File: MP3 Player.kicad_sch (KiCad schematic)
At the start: 48 parts, among them J1 Conn_01x02_Pin, J2 USB_C_Receptacle_USB2.0_14P, J3 SJ2-3574A-SMT-TR, J4 Conn_01x02_Pin, J5 1051620001, J6 Conn_01x04_Pin, Q1 IRLML6402, SW1 SW_SPDT, SW2 SW_MEC_5E, SW3 SW_MEC_5E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

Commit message: Cleaned up the schematic
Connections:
- net +3V3: no longer SW5.3 (K), SW5.4 (A), SW6.3 (K), SW6.4 (A), SW7.3 (K), SW7.4 (A), SW8.3 (K), SW8.4 (A)
- net HPL: no longer C7.1, J3.2
- net HRP: no longer C8.1, J3.3
- new net: SW7.3 (K), SW7.4 (A)
- new net: C7.1, J3.2
- new net: SW5.3 (K), SW5.4 (A)
- new net: SW6.3 (K), SW6.4 (A)
- new net: SW8.3 (K), SW8.4 (A)
- new net: C8.1, J3.3
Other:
- moved on the sheet: C7, C8, J6, R10, R11, R12, R13, R14, SW4, SW5, SW6, SW7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

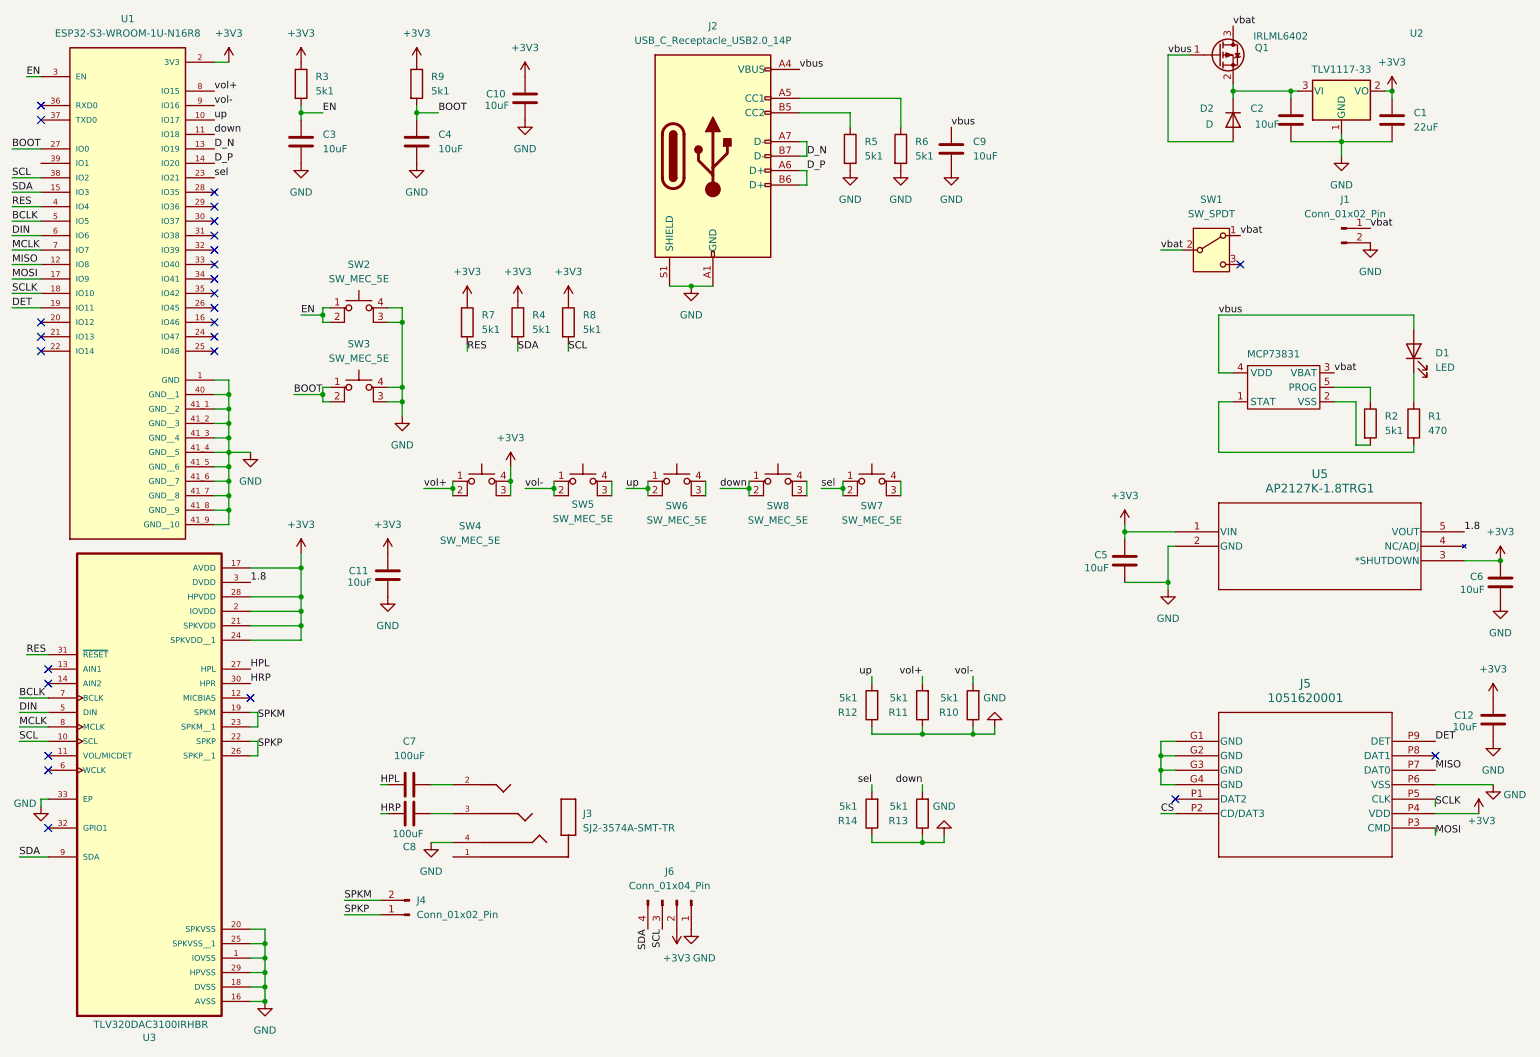
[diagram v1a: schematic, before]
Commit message: Cleaned up schematic
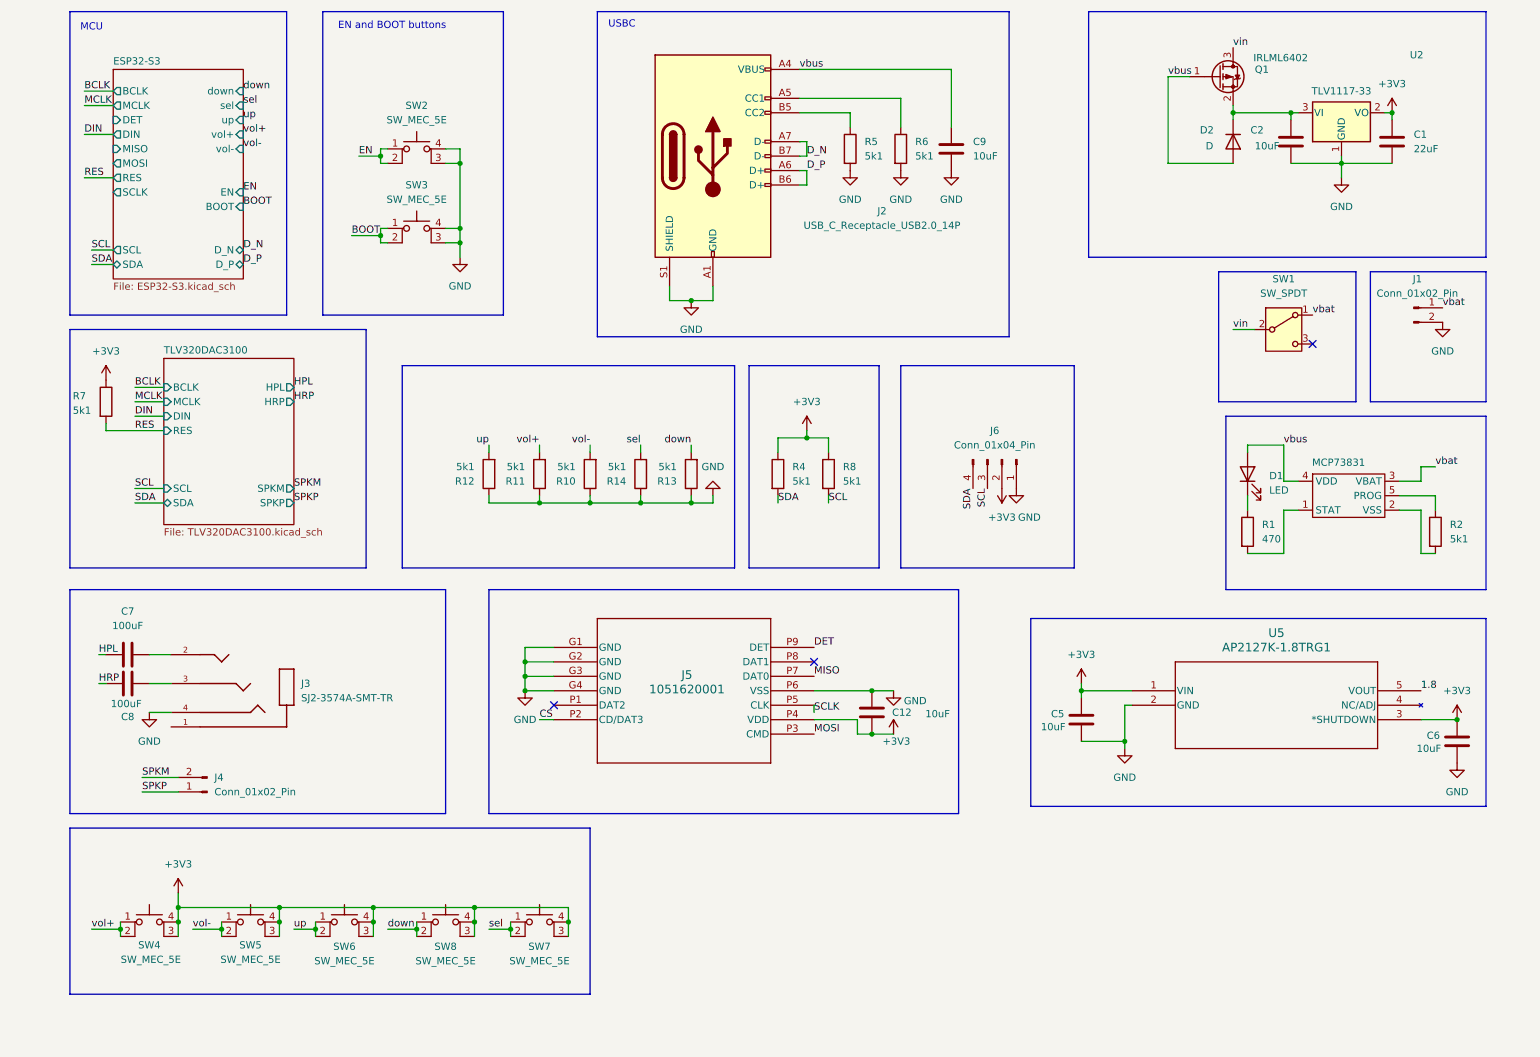
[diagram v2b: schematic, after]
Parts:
- removed C10, C11, C3, C4: 10uF, Capacitor_SMD:C_0805_2012Metric, symbol Device:C
- removed R3, R9: 5k1, Resistor_SMD:R_0805_2012Metric, symbol Device:R
- removed U1: ESP32-S3-WROOM-1U-N16R8, ESP32_S3_WROOM_1U_N16R8:XCVR_ESP32-S3-WROOM-1U-N16R8, symbol ESP32-S3-WROOM-1U-N16R8:ESP32-S3-WROOM-1U-N16R8
- removed U3: TLV320DAC3100IRHBR, TLV320DAC3100IRHBR:IC_ADS125H01IRHBT, symbol TLV320DAC3100IRHBR:TLV320DAC3100IRHBR
- D1: footprint Diode_SMD:D_0603_1608Metric -> (none)
- R1: footprint Resistor_SMD:R_0805_2012Metric -> (none)
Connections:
- net +3V3: now also C12.2, SW5.3 (K), SW5.4 (A), SW6.3 (K), SW6.4 (A), SW7.3 (K), SW7.4 (A), SW8.3 (K), SW8.4 (A); no longer C12.1
- net GND: now also C12.1, J5.G1 (GND), J5.G2 (GND), J5.G3 (GND), J5.G4 (GND); no longer C12.2
- net vbat: no longer Q1.3 (D), SW1.2 (B)
- new net vin: Q1.3 (D), SW1.2 (B)
- no-connect marks 26 -> 3
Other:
- added sheet ESP32-S3 (ESP32-S3.kicad_sch)
- added sheet TLV320DAC3100 (TLV320DAC3100.kicad_sch)
- note added: "EN and BOOT buttons"
- note added: "MCU"
- note added: "USBC"
- moved on the sheet: C1, C12, C2, C5, C6, C7, C8, D2, J1, J3, J4, J5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

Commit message: updated board design
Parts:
- D1: footprint (none) -> LED_SMD:LED_0603_1608Metric_Pad1.05x0.95mm_HandSolder
- R1: footprint (none) -> Resistor_SMD:R_0805_2012Metric
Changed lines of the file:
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@@
 			)
 		)
-		(property "Footprint" ""
+		(property "Footprint" "LED_SMD:LED_0603_1608Metric_Pad1.05x0.95mm_HandSolder"
 			(at 229.87 96.52 0)
 			(hide yes)
@@
 			)
 		)
-		(property "Footprint" ""
+		(property "Footprint" "Resistor_SMD:R_0805_2012Metric"
 			(at 228.092 106.68 90)
 			(hide yes)

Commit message: updated board design to fit altoid tin
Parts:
- removed SW2, SW3: SW_MEC_5E, Button_Switch_THT:SW_PUSH_6mm, symbol Switch:SW_MEC_5E
- added SW10, SW9: SW_MEC_5E, Button_Switch_SMD:Panasonic_EVQPUK_EVQPUB, symbol Switch:SW_MEC_5E
- J1: footprint Connector_PinHeader_1.00mm:PinHeader_1x02_P1.00mm_Vertical -> Connector_PinHeader_2.54mm:PinHeader_1x02_P2.54mm_Vertical
- J3: footprint SJ2_3574A_SMT_TR:SAMESKY_SJ2-3574A-SMT-TR -> 35RASMT4BHNTRX:35RASMT4BHNTRX_SWC
- J5: footprint 105162-0001_MOL -> 35RASMT4BHNTRX:105162-0001_MOL
- MCP73831: footprint MCP73831:SOT-23-5_MC_MCH -> footprints:SOT-23-5_AP2127K_DIO
- SW4, SW5, SW6, SW7, SW8: footprint Button_Switch_THT:SW_PUSH_6mm -> Button_Switch_SMD:Panasonic_EVQPUK_EVQPUB
- U2: footprint TLV1117LV33DCYR:VREG_TLV1117LV33DCYR -> TLV1117:DCY0004A_L
- U5: footprint SOT-23-5_AP2127K_DIO -> footprints:SOT-23-5_AP2127K_DIO
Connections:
- net +3V3: now also SW4.1, SW5.1, SW6.1, SW7.1, SW8.1; no longer SW4.3 (K), SW4.4 (A), SW5.3 (K), SW5.4 (A), SW6.3 (K), SW6.4 (A), SW7.3 (K), SW7.4 (A), SW8.3 (K), SW8.4 (A)
- net BOOT: now also SW10.2
- net EN: now also SW9.2
- net GND: now also SW10.1, SW9.1
- net down: now also SW7.2; no longer SW8.1, SW8.2
- net sel: now also SW8.2; no longer SW7.1, SW7.2
- net up: no longer SW6.1
- net vol+: no longer SW4.1
- net vol-: no longer SW5.1
- net D_N renamed USB_N
- net D_P renamed USB_P
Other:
- sheet ESP32-S3 ports: added CS; removed none
- sheet TLV320DAC3100 ports: added DVDD; removed none
